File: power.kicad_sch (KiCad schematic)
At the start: 32 parts, among them J7 USB-C_GCT_USB4105-GF-A, J8 Molex_Nano-Fit_1x2_SMD_105430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, U10 TPS564247DRLR, U6 TPS564247DRLR, U7 TPS564247DRLR, U8 TPS564247DRLR, U9 TPS564247DRLR

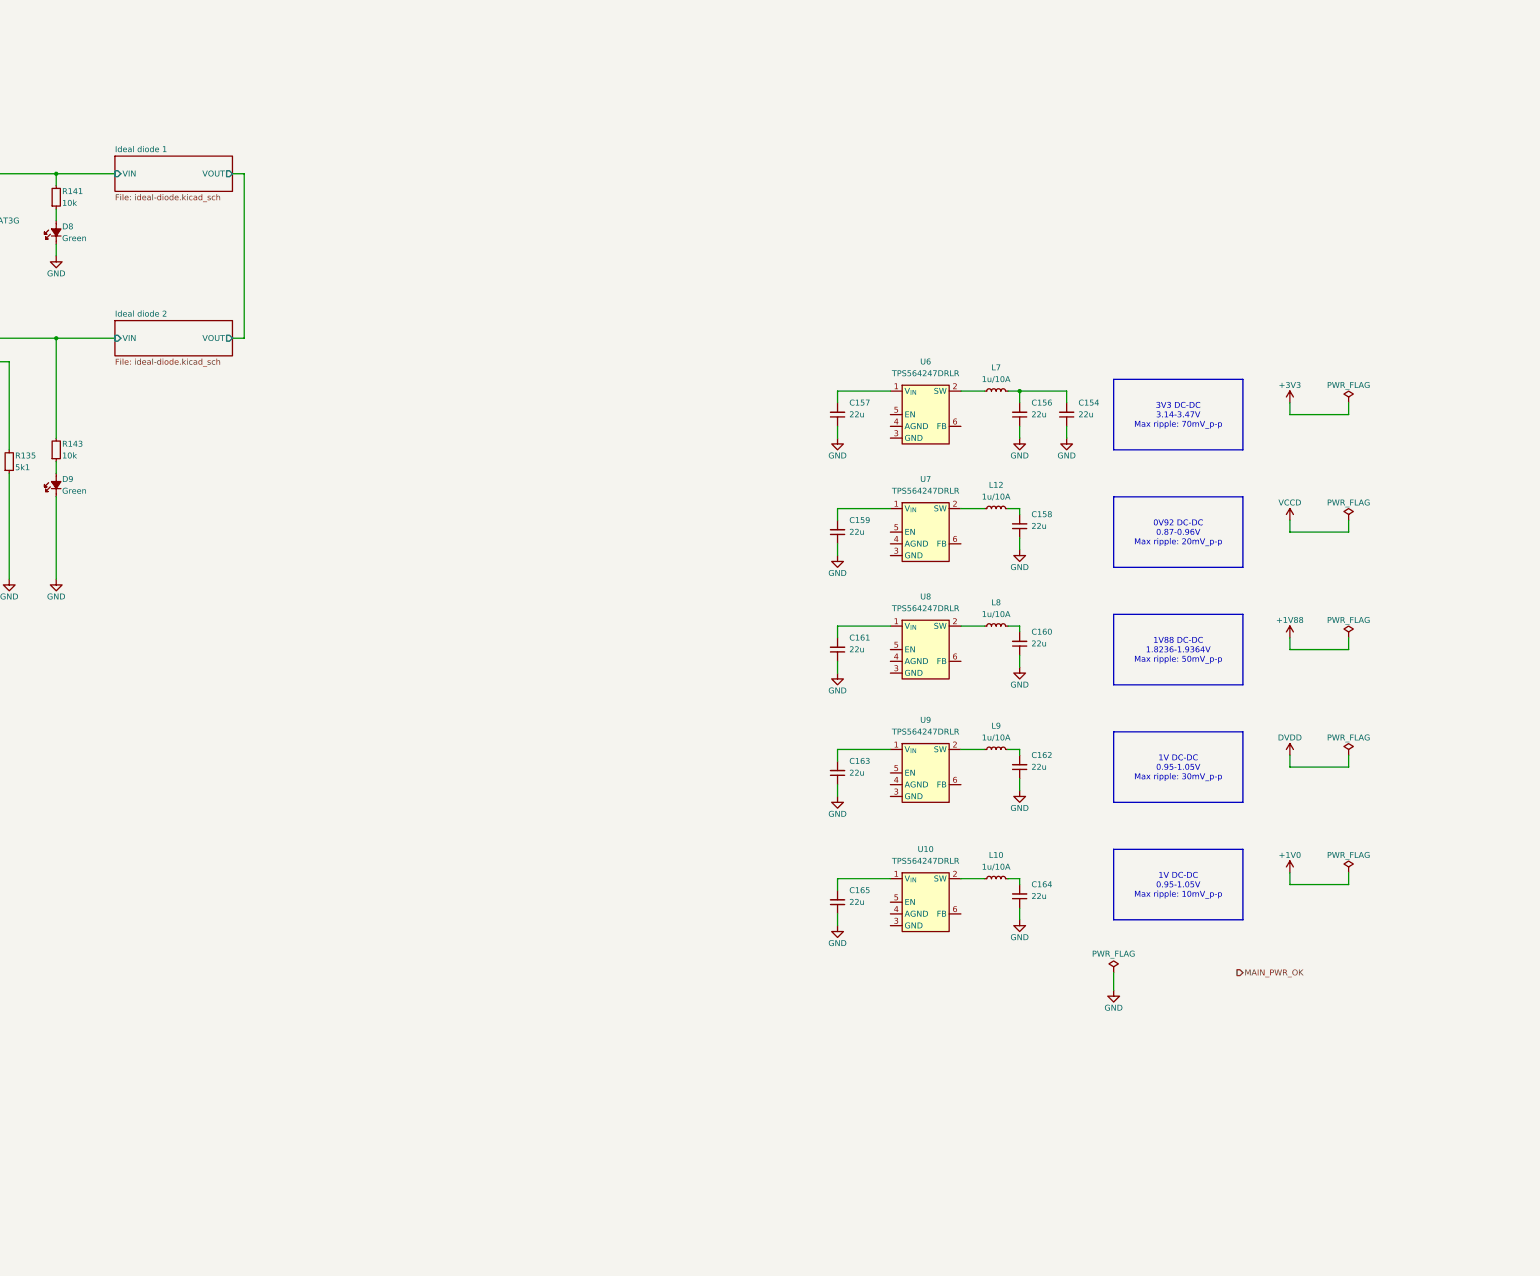
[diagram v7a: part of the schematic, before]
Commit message: [#81595] Create DC-DC converters schematic section
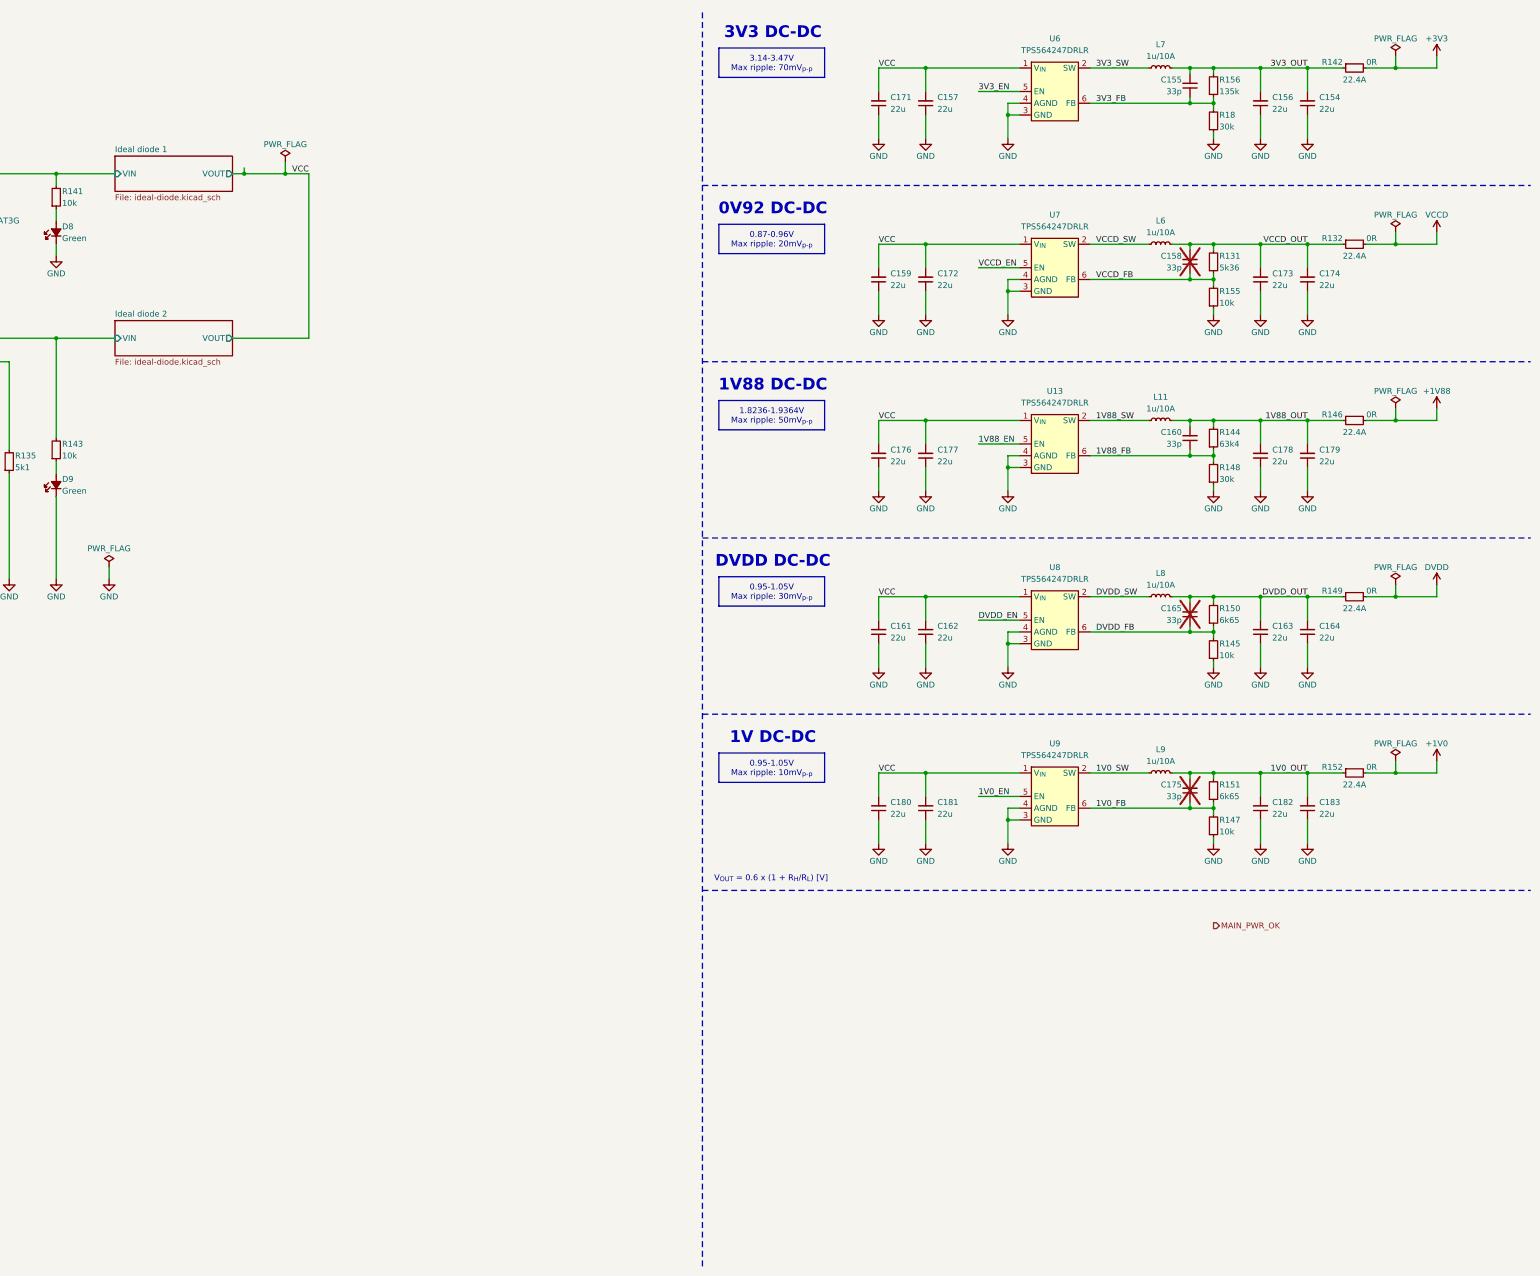
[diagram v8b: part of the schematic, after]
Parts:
- removed C158, C160, C165: C_22u_16V_0603, antmicro-footprints:C_0603_1608Metric_EIA, symbol antmicroCapacitors0603:C_22u_16V_0603
- removed L10, L12: L_1u_10A_Bourns-SRP4021HMT, antmicro-footprints:L_Bourns-SRP4021HMT, symbol antmicroFixedInductors:L_1u_10A_Bourns-SRP4021HMT
- removed U10: TPS564247DRLR, antmicro-footprints:SOT-563, symbol antmicroDCDCConverters:TPS564247DRLR
- added C155, C158, C160, C165, C175: C_33p_0402, antmicro-footprints:C_0402_1005Metric, symbol antmicroCapacitors0402:C_33p_0402
- added C171, C172, C173, C174, C176, C177, C178, C179, C180, C181, C182, C183: C_22u_16V_0603, antmicro-footprints:C_0603_1608Metric_EIA, symbol antmicroCapacitors0603:C_22u_16V_0603
- added L11, L6: L_1u_10A_Bourns-SRP4021HMT, antmicro-footprints:L_Bourns-SRP4021HMT, symbol antmicroFixedInductors:L_1u_10A_Bourns-SRP4021HMT
- added R131: R_5k36_0402, antmicro-footprints:R_0402_1005Metric, symbol antmicroResistors0402:R_5k36_0402
- added R132, R142, R146, R149, R152: R_0R_22.4A_0603, antmicro-footprints:R_0603_1608Metric, symbol antmicroResistors0603:R_0R_22.4A_0603
- added R144: R_63k4_0402, antmicro-footprints:R_0402_1005Metric, symbol antmicroResistors0402:R_63k4_0402
- added R145, R147, R155: R_10k_0.1%_0402, antmicro-footprints:R_0402_1005Metric, symbol antmicroResistors0402:R_10k_0.1%_0402
- added R148, R18: R_30k_0402, antmicro-footprints:R_0402_1005Metric, symbol antmicroResistors0402:R_30k_0402
- added R150, R151: R_6k65_0402, antmicro-footprints:R_0402_1005Metric, symbol antmicroResistors0402:R_6k65_0402
- added R156: R_135k_0402, antmicro-footprints:R_0402_1005Metric, symbol antmicroResistors0402:R_135k_0402
- added U13: TPS564247DRLR, antmicro-footprints:SOT-563, symbol antmicroDCDCConverters:TPS564247DRLR
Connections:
- net +1V0: now also R152.2
- net +1V88: now also R146.2
- net +3V3: now also R142.2
- net DVDD: now also R149.2
- net GND: now also U6.3 (GND), U6.4 (AGND), U7.3 (GND), U7.4 (AGND), U8.3 (GND), U8.4 (AGND), U9.3 (GND), U9.4 (AGND), C171.1, C172.1, C173.1, C174.1, C176.1, C177.1, C178.1, C179.1, C180.1, C181.1, C182.1, C183.1, R145.1, R147.1, R148.1, R155.1, R18.1, U13.3 (GND), U13.4 (AGND)
- net VCCD: now also R132.2
- net 3V3_OUT: now reaches C154.2, C156.2, L7.2
- net 3V3_OUT: now also C155.2, R142.1, R156.2
- net 1V0_OUT: now reaches L9.2
- net 1V0_OUT: now also C175.2, C182.2, C183.2, R151.2, R152.1; no longer C162.2
- net 1V0_SW: now reaches L9.1, U9.2 (SW)
- net DVDD_SW: now reaches L8.1, U8.2 (SW)
- net DVDD_OUT: now reaches L8.2
- net DVDD_OUT: now also C163.2, C164.2, C165.2, R149.1, R150.2
- net VCCD_SW: now reaches U7.2 (SW)
- net VCCD_SW: now also L6.1
- net VCC: now reaches C159.2, U7.1 (V_{IN})
- net VCC: now also C157.2, C161.2, C162.2, U6.1 (V_{IN}), U8.1 (V_{IN}), U9.1 (V_{IN}), C171.2, C172.2, C176.2, C177.2, C180.2, C181.2, U13.1 (V_{IN})
- net DVDD_EN: now reaches U8.5 (EN)
- net DVDD_FB: now reaches U8.6 (FB)
- net DVDD_FB: now also C165.1, R145.2, R150.1
- net 3V3_SW: now reaches L7.1, U6.2 (SW)
- net 3V3_EN: now reaches U6.5 (EN)
- net 3V3_FB: now reaches U6.6 (FB)
- net 3V3_FB: now also C155.1, R156.1, R18.2
- net VCCD_EN: now reaches U7.5 (EN)
- net VCCD_FB: now reaches U7.6 (FB)
- net VCCD_FB: now also C158.1, R131.1, R155.2
- net 1V0_EN: now reaches U9.5 (EN)
- net 1V0_FB: now reaches U9.6 (FB)
- net 1V0_FB: now also C175.1, R147.2, R151.1
- new net 1V88_EN: U13.5 (EN)
- new net 1V88_FB: C160.1, R144.1, R148.2, U13.6 (FB)
- new net 1V88_OUT: C160.2, C178.2, C179.2, L11.2, R144.2, R146.1
- new net 1V88_SW: L11.1, U13.2 (SW)
- new net VCCD_OUT: C158.2, C173.2, C174.2, L6.2, R131.2, R132.1
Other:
- note added: "0V92 DC-DC"
- note added: "1V DC-DC"
- note added: "1V88 DC-DC"
- note added: "3V3 DC-DC"
- note added: "DVDD DC-DC"
- note added: "V_{OUT} = 0.6 x (1 + R_{H}/R_{L}) [V]"
- moved on the sheet: C154, C156, C157, L7, U6
